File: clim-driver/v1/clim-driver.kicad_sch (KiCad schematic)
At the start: 10 parts, among them J1 Conn_01x03_Male, J2 Conn_01x02_Pin, J5 Screw_Terminal_01x02, Q1 BSS138, U2 WeMos_D1_mini

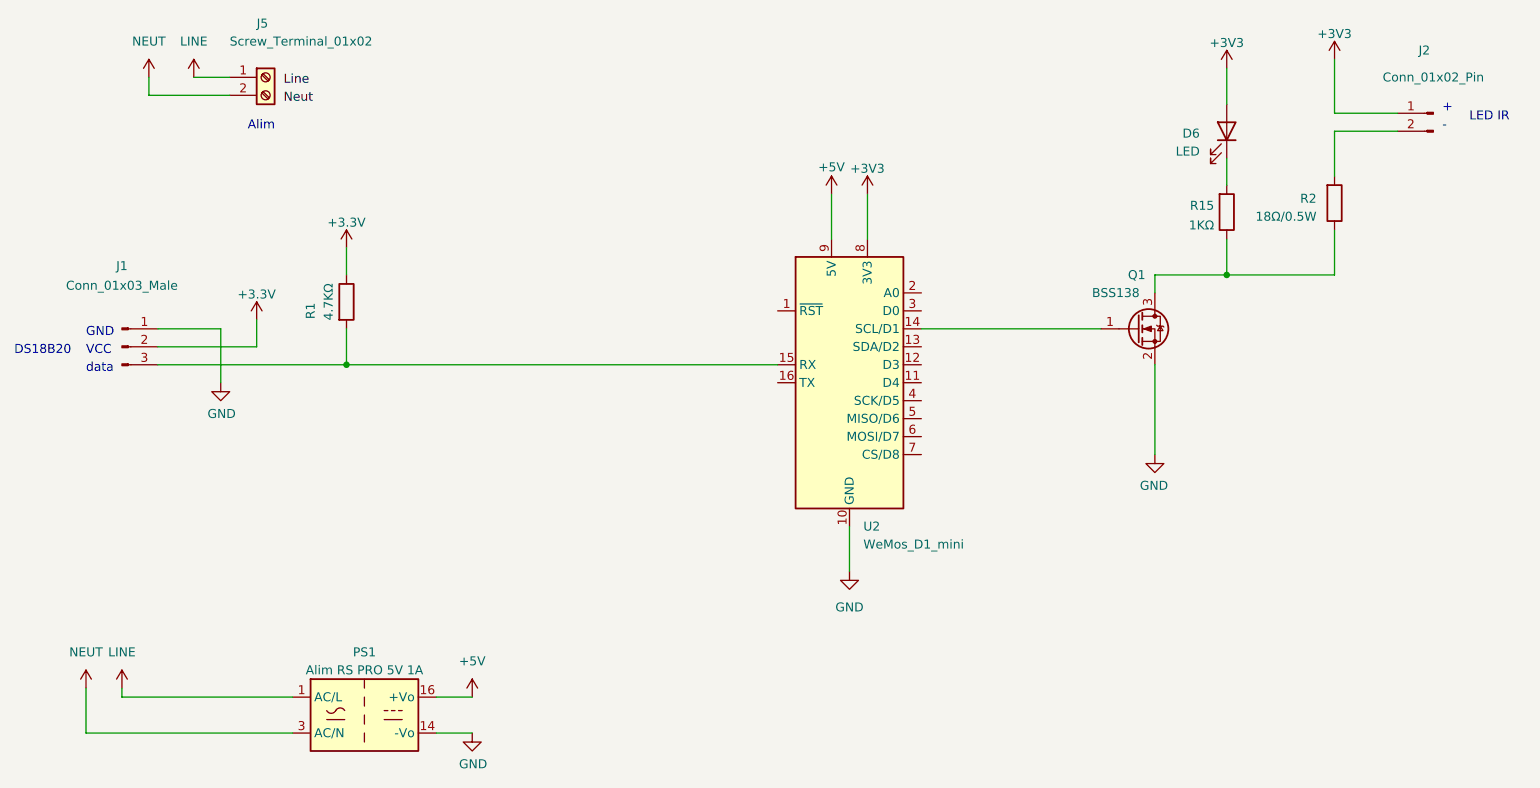
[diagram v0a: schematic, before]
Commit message: update schematic
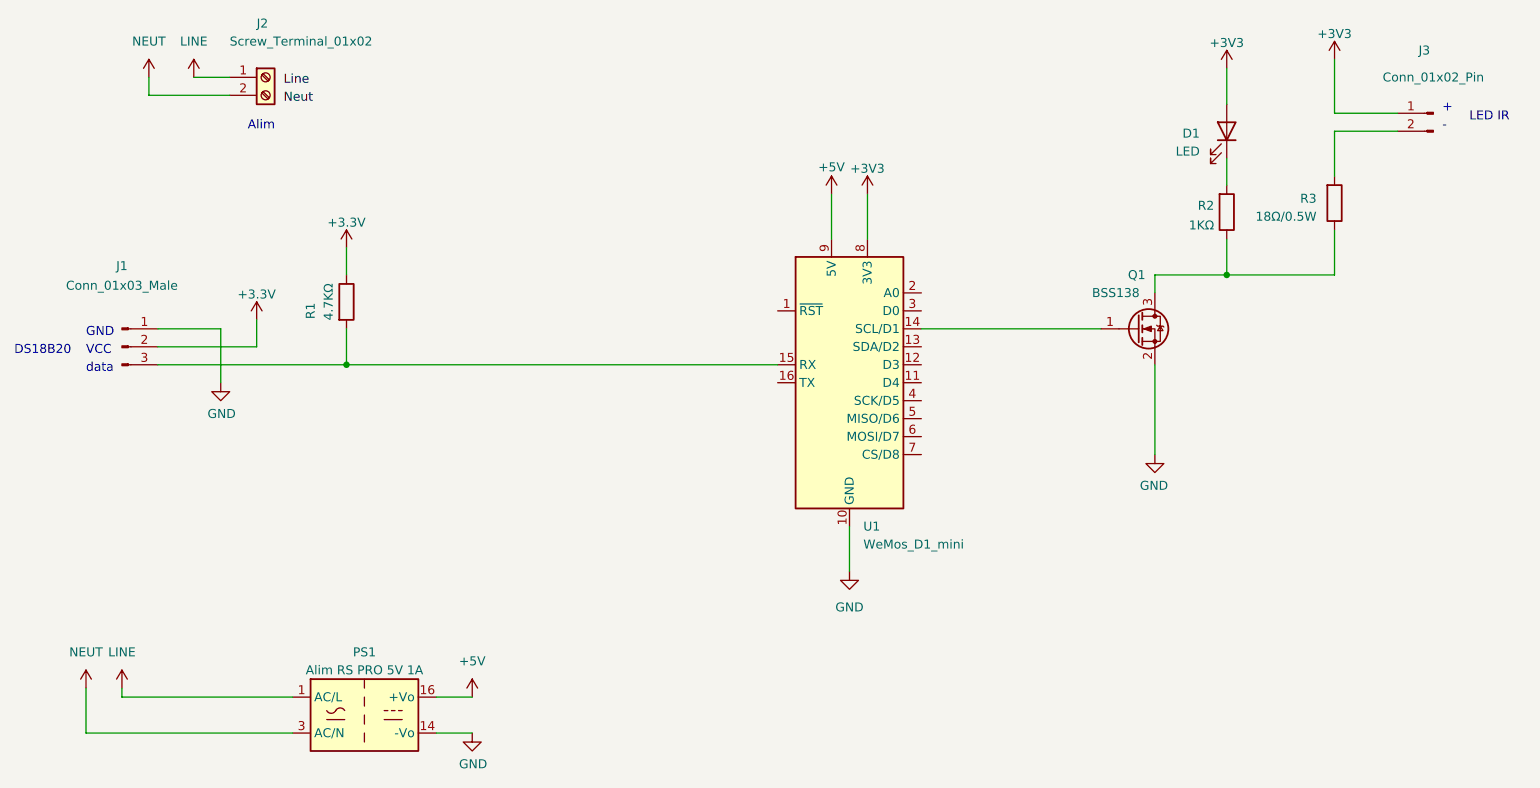
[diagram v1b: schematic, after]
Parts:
- J3: renamed from J2; footprint (none) -> Connector_PinHeader_2.54mm:PinHeader_1x02_P2.54mm_Vertical
- R3: renamed from R2; footprint (none) -> Resistor_SMD:R_1210_3225Metric; LCSC (none) -> C333138
- renumbered D6 to D1, J5 to J2, R15 to R2, U2 to U1

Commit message: wip pcb
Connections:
- net LINE: now also J2.2 (Pin_2); no longer J2.1 (Pin_1)
- net NEUT: now also J2.1 (Pin_1); no longer J2.2 (Pin_2)
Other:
- moved on the sheet: J2
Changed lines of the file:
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@@
+    (stroke (width 0) (type default))
+  )
+  (wire (pts (xy 58.42 55.88) (xy 60.96 55.88))
     (stroke (width 0) (type default))
   )
@@
     (stroke (width 0) (type default))
   )
-  (wire (pts (xy 63.5 58.42) (xy 52.07 58.42))
+  (wire (pts (xy 52.07 58.42) (xy 60.96 58.42))
     (stroke (width 0) (type default))
   )
@@
   )
   (wire (pts (xy 204.47 54.61) (xy 204.47 59.69))
-    (stroke (width 0) (type default))
-  )
-  (wire (pts (xy 58.42 55.88) (xy 63.5 55.88))
     (stroke (width 0) (type default))
   )
@@
     )
   )
-  (symbol (lib_id "Connector:Screw_Terminal_01x02") (at 68.58 55.88 0) (unit 1)
+  (symbol (lib_id "Connector:Screw_Terminal_01x02") (at 66.04 58.42 0) (mirror x) (unit 1)
     (in_bom yes) (on_board yes) (dnp no)
-    (property "Reference" "J2" (at 67.31 48.26 0)
+    (property "Reference" "J2" (at 64.77 49.53 0)
       (effects (font (size 1.27 1.27)) (justify left))
     )
-    (property "Value" "Screw_Terminal_01x02" (at 63.5 50.8 0)
+    (property "Value" "Screw_Terminal_01x02" (at 63.5 52.07 0)
       (effects (font (size 1.27 1.27)) (justify left))
     )
-    (property "Footprint" "TerminalBlock:TerminalBlock_bornier-2_P5.08mm" (at 68.58 55.88 0)
-      (effects (font (size 1.27 1.27)) hide)
-    )
-    (property "Datasheet" "~" (at 68.58 55.88 0)
-      (effects (font (size 1.27 1.27)) hide)
-    )
+    (property "Footprint" "TerminalBlock:TerminalBlock_bornier-2_P5.08mm" (at 66.04 58.42 0)
+      (effects (font (size 1.27 1.27)) hide)
+    )
+    (property "Datasheet" "~" (at 66.04 58.42 0)
+      (effects (font (size 1.27 1.27)) hide)
+    )
